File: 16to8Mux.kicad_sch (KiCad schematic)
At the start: 4 parts

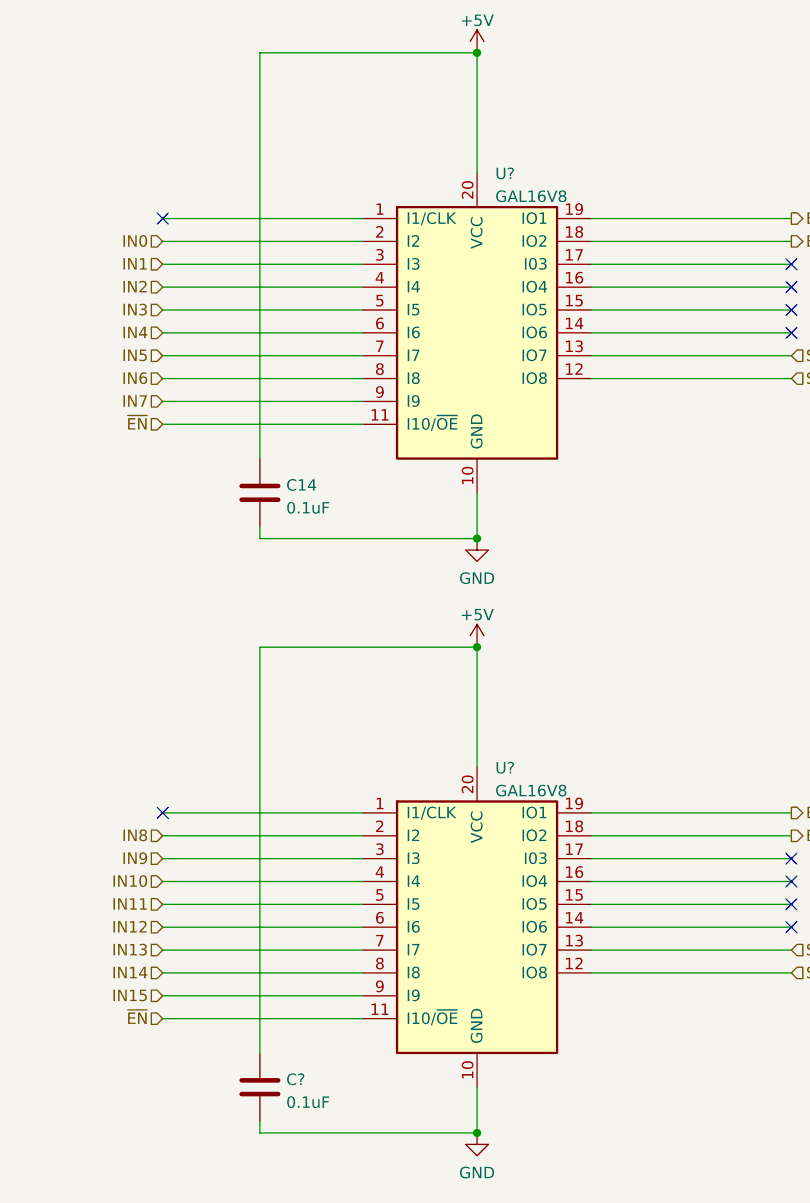
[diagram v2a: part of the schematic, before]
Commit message: Added a breakout of the management engine pins
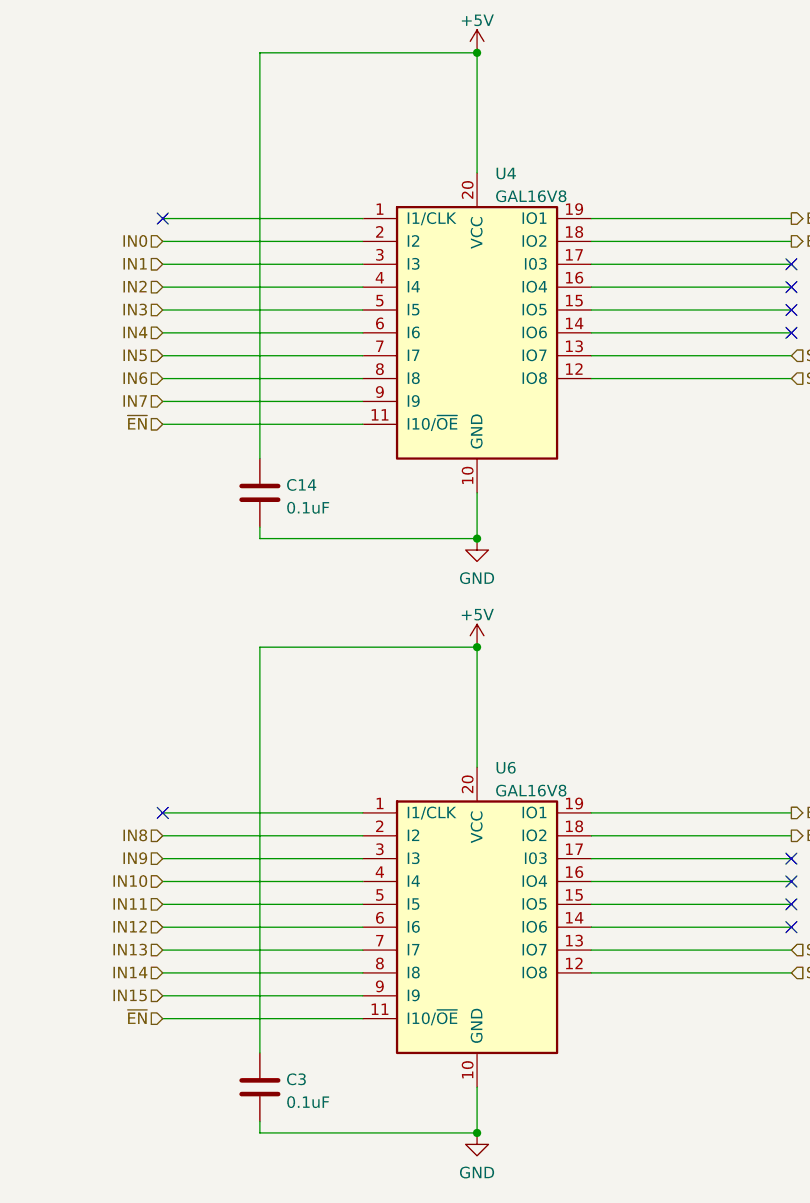
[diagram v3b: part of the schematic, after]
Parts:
- gave numbers to parts that had none: 3
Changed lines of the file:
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@@
   (symbol (lib_id "Logic_Programmable:GAL16V8") (at 174.625 66.04 0) (unit 1)
     (in_bom yes) (on_board yes) (fields_autoplaced)
-    (property "Reference" "U?" (id 0) (at 176.6444 48.3702 0)
+    (property "Reference" "U4" (id 0) (at 176.6444 48.3702 0)
       (effects (font (size 1.27 1.27)) (justify left))
     )
@@
   (symbol (lib_id "power:GND") (at 174.625 154.94 0) (unit 1)
     (in_bom yes) (on_board yes) (fields_autoplaced)
-    (property "Reference" "#PWR?" (id 0) (at 174.625 161.29 0)
+    (property "Reference" "#PWR061" (id 0) (at 174.625 161.29 0)
       (effects (font (size 1.27 1.27)) hide)
     )
@@
   (symbol (lib_id "Device:C") (at 150.495 149.86 0) (unit 1)
     (in_bom yes) (on_board yes) (fields_autoplaced)
-    (property "Reference" "C?" (id 0) (at 153.416 149.0253 0)
+    (property "Reference" "C3" (id 0) (at 153.416 149.0253 0)
       (effects (font (size 1.27 1.27)) (justify left))
     )
@@
   (symbol (lib_id "power:+5V") (at 174.625 100.965 0) (unit 1)
     (in_bom yes) (on_board yes) (fields_autoplaced)
-    (property "Reference" "#PWR?" (id 0) (at 174.625 104.775 0)
+    (property "Reference" "#PWR060" (id 0) (at 174.625 104.775 0)
       (effects (font (size 1.27 1.27)) hide)
     )
@@
   (symbol (lib_id "Logic_Programmable:GAL16V8") (at 174.625 132.08 0) (unit 1)
     (in_bom yes) (on_board yes) (fields_autoplaced)
-    (property "Reference" "U?" (id 0) (at 176.6444 114.4102 0)
+    (property "Reference" "U6" (id 0) (at 176.6444 114.4102 0)
       (effects (font (size 1.27 1.27)) (justify left))
     )
